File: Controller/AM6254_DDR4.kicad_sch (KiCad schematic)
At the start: 36 parts, among them U11 AM6252ASGFHIAMCRQ1, U5 MT40A1G16WBU-083E_B

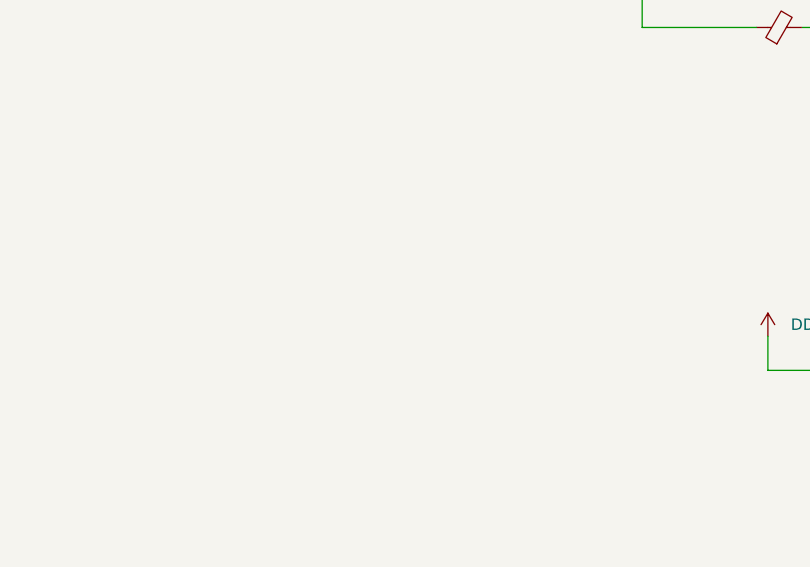
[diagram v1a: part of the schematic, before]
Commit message: DDR_CLK termination
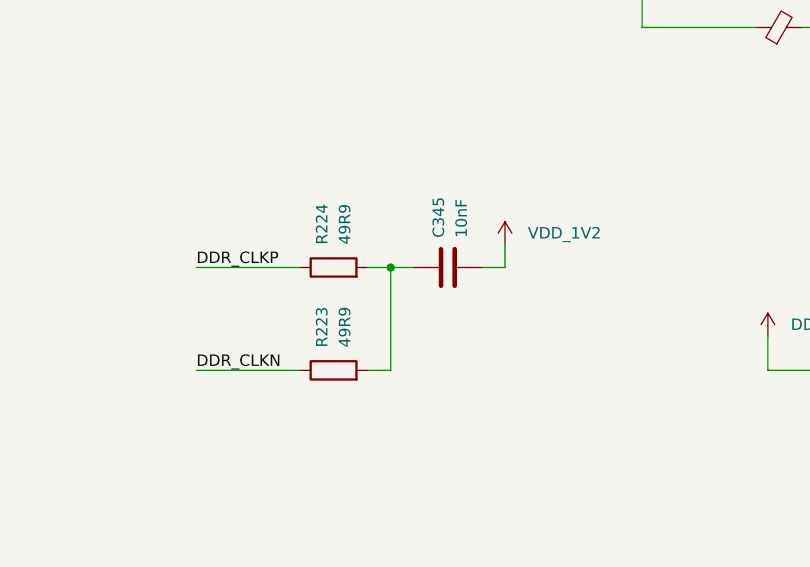
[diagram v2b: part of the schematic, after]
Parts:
- added C345: 10nF, Capacitor_SMD:C_0402_1005Metric, symbol Device:C
- added R223, R224: 49R9, Resistor_SMD:R_0402_1005Metric, symbol Device:R
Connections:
- net DDR_CLKN: now also R223.1
- net DDR_CLKP: now also R224.1
- net VDD_1V2: now also C345.2
- new net: C345.1, R223.2, R224.2

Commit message: Testpoints + DDR velocity comp
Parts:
- added TP17: TestPoint, TestPoint:TestPoint_Pad_D1.0mm, symbol Connector:TestPoint
- R158: now not fitted
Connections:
- net DDR_RESET: now also TP17.1
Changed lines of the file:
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@@
 	(wire
 		(pts
+			(xy 142.24 157.48) (xy 142.24 160.02)
+		)
+		(stroke
+			(width 0)
+			(type default)
+		)
+	)
+	(wire
+		(pts
 			(xy 262.89 50.8) (xy 262.89 53.34)
 		)
@@
 	(wire
 		(pts
+			(xy 142.24 160.02) (xy 147.32 160.02)
+		)
+		(stroke
+			(width 0)
+			(type default)
+		)
+	)
+	(wire
+		(pts
 			(xy 342.9 35.56) (xy 342.9 38.1)
 		)
@@
 	)
 	(symbol
+		(lib_id "Connector:TestPoint")
+		(at 142.24 157.48 0)
+		(mirror y)
+		(unit 1)
+		(body_style 1)
+		(exclude_from_sim no)
+		(in_bom yes)
+		(on_board yes)
+		(in_pos_files yes)
+		(dnp no)
+		(property "Reference" "TP17"
+			(at 139.7 152.9079 0)
+			(show_name no)
+			(do_not_autoplace no)
+			(effects
+				(font
+					(size 1.27 1.27)
+				)
+				(justify left)
+			)
+		)
+		(property "Value" "TestPoint"
+			(at 139.7 155.4479 0)
+			(show_name no)
+			(do_not_autoplace no)
+			(effects
+				(font
+					(size 1.27 1.27)
+				)
+				(justify left)
+			)
+		)
+		(property "Footprint" "TestPoint:TestPoint_Pad_D1.0mm"
+			(at 137.16 157.48 0)
+			(hide yes)
+			(show_name no)
+			(do_not_autoplace no)
+			(effects
+				(font
+					(size 1.27 1.27)
+				)
+			)
+		)
+		(property "Datasheet" ""
+			(at 137.16 157.48 0)
+			(hide yes)
+			(show_name no)
+			(do_not_autoplace no)
+			(effects
+				(font
+					(size 1.27 1.27)
+				)
+			)
+		)
+		(property "Description" "test point"
+			(at 142.24 157.48 0)
+			(hide yes)
+			(show_name no)
+			(do_not_autoplace no)
+			(effects
+				(font
+					(size 1.27 1.27)
+				)
+			)
+		)
+		(pin "1"
+		)
+		(instances
+			(project "Controller"
+				(path "/2c9e7a41-63e4-4339-89dd-991e772f7a19/744ffe61-5260-41ff-b05d-255b0f5e8531"
+					(reference "TP17")
+					(unit 1)
+				)
+			)
+		)
+	)
+	(symbol
 		(lib_id "Device:C")
 		(at 292.1 57.15 0)
@@
 		(on_board yes)
 		(in_pos_files yes)
-		(dnp no)
+		(dnp yes)
 		(fields_autoplaced yes)
 		(property "Reference" "R158"
